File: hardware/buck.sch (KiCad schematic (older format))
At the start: 13 parts, among them U5 MP1584EN

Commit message: fix a silk screen error by swapping R14 and R15
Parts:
- renumbered R15 to R14, R14 to R15
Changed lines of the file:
@@
 P 4200 2500
 AR Path="/5C3476D8/5CA62D89" Ref="R?"  Part="1"
-AR Path="/5CA65CC5/5CA62D89" Ref="R14"  Part="1"
-F 0 "R14" H 4270 2546 50  0000 L CNN
+AR Path="/5CA65CC5/5CA62D89" Ref="R15"  Part="1"
+F 0 "R15" H 4270 2546 50  0000 L CNN
 F 1 "40.2k" H 4270 2455 50  0000 L CNN
 F 2 "Resistor_SMD:R_0603_1608Metric_Pad1.05x0.95mm_HandSolder" V 4130 2500 50  0001 C CNN
@@
 P 4550 2350
 AR Path="/5C3476D8/5CA62D90" Ref="R?"  Part="1"
-AR Path="/5CA65CC5/5CA62D90" Ref="R15"  Part="1"
-F 0 "R15" V 4757 2350 50  0000 C CNN
+AR Path="/5CA65CC5/5CA62D90" Ref="R14"  Part="1"
+F 0 "R14" V 4757 2350 50  0000 C CNN
 F 1 "210k" V 4666 2350 50  0000 C CNN
 F 2 "Resistor_SMD:R_0603_1608Metric_Pad1.05x0.95mm_HandSolder" V 4480 2350 50  0001 C CNN

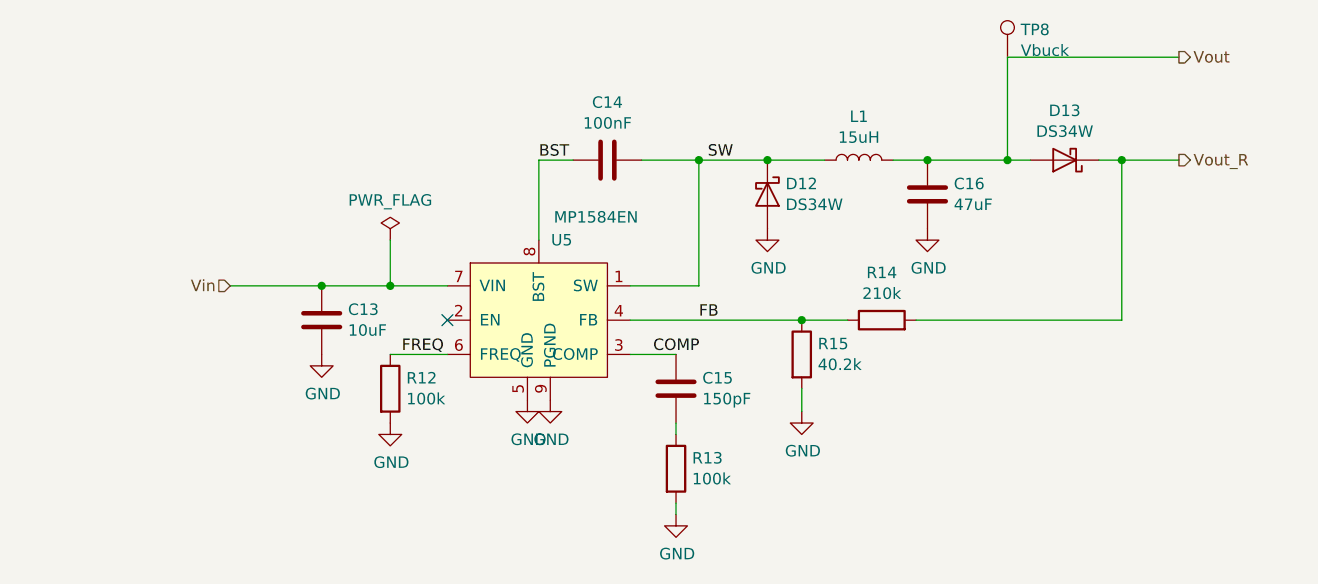
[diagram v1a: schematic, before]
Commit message: Changed to pure-serial topology. Changed to beefier mcu.
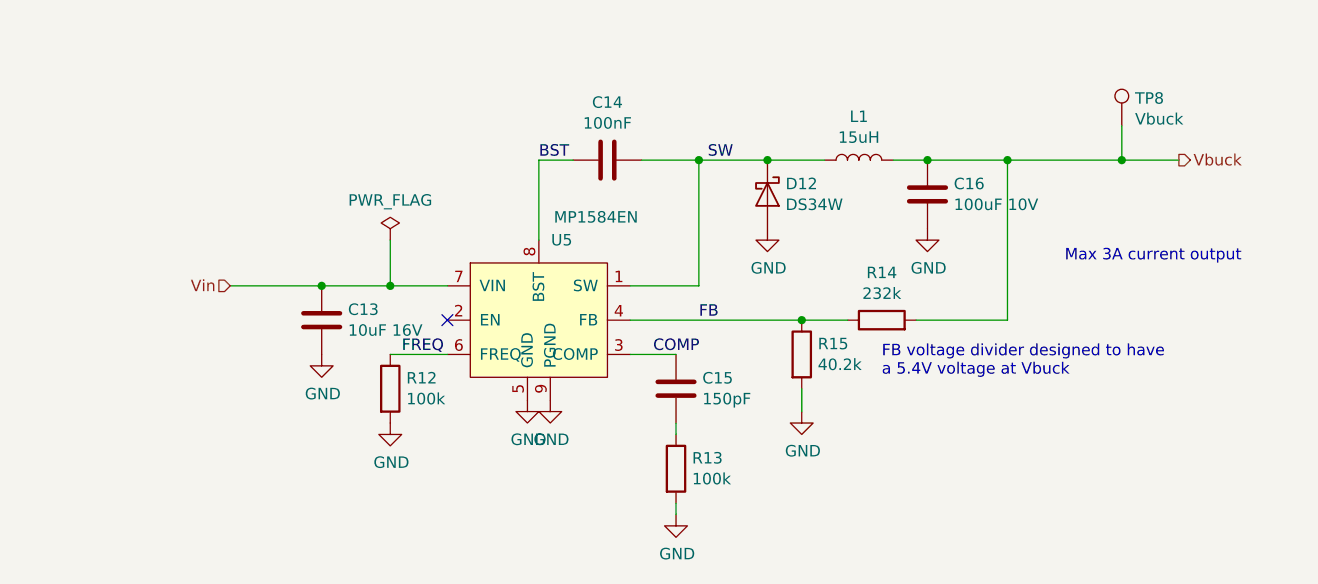
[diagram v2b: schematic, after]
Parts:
- removed D13: DS34W, Diode_SMD:D_SOD-123F, symbol Device:D_Schottky
- C13: value 10uF -> 10uF 16V
- C16: value 47uF -> 100uF 10V; footprint Capacitor_SMD:C_0805_2012Metric_Pad1.15x1.40mm_HandSolder -> Capacitor_SMD:C_1210_3225Metric_Pad1.42x2.65mm_HandSolder
- R14: value 210k -> 232k
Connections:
- net Vout_R is gone; now on net Vbuck: R14.2
- net Vout renamed Vbuck
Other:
- note added: "FB voltage divider designed to have\na 5.4V voltage at Vbuck"
- note added: "Max 3A current output"
- moved on the sheet: TP8
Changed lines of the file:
@@
-EESchema Schematic File Version 4
+EESchema Schematic File Version 5
 LIBS:pi-supercap-ups-cache
-EELAYER 26 0
+EELAYER 30 0
 EELAYER END
 $Descr A4 11693 8268
 encoding utf-8
-Sheet 6 8
+Sheet 8 8
 Title ""
 Date ""
@@
 AR Path="/5CA65CC5/5CA62D4C" Ref="C13"  Part="1"
 F 0 "C13" H 2215 2396 50  0000 L CNN
-F 1 "10uF" H 2215 2305 50  0000 L CNN
+F 1 "10uF 16V" H 2215 2305 50  0000 L CNN
 F 2 "Capacitor_SMD:C_0805_2012Metric_Pad1.15x1.40mm_HandSolder" H 2138 2200 50  0001 C CNN
 F 3 "~" H 2100 2350 50  0001 C CNN
@@
 AR Path="/5CA65CC5/5CA62D82" Ref="C16"  Part="1"
 F 0 "C16" H 4865 1846 50  0000 L CNN
-F 1 "47uF" H 4865 1755 50  0000 L CNN
-F 2 "Capacitor_SMD:C_0805_2012Metric_Pad1.15x1.40mm_HandSolder" H 4788 1650 50  0001 C CNN
+F 1 "100uF 10V" H 4865 1755 50  0000 L CNN
+F 2 "Capacitor_SMD:C_1210_3225Metric_Pad1.42x2.65mm_HandSolder" H 4788 1650 50  0001 C CNN
 F 3 "~" H 4750 1800 50  0001 C CNN
 F 4 "Min 6.3V" H 4750 1800 50  0001 C CNN "Notes"
@@
 AR Path="/5CA65CC5/5CA62D90" Ref="R14"  Part="1"
 F 0 "R14" V 4757 2350 50  0000 C CNN
-F 1 "210k" V 4666 2350 50  0000 C CNN
+F 1 "232k" V 4666 2350 50  0000 C CNN
 F 2 "Resistor_SMD:R_0603_1608Metric_Pad1.05x0.95mm_HandSolder" V 4480 2350 50  0001 C CNN
 F 3 "~" H 4550 2350 50  0001 C CNN
@@
 	3450 2350 4200 2350
 Wire Wire Line
-	4700 2350 5600 2350
+	4700 2350 5100 2350
 Wire Wire Line
 	3750 1650 3750 2200
-Wire Wire Line
-	5600 1650 5600 2350
 Wire Wire Line
 	3500 1650 3750 1650
@@
 Wire Wire Line
 	4200 2350 4400 2350
-Connection ~ 5600 1650
-Wire Wire Line
-	5600 1650 5850 1650
 Connection ~ 4050 1650
 Wire Wire Line
@@
 Text HLabel 1700 2200 0    50   Input ~ 0
 Vin
-$Comp
-L Device:D_Schottky D?
-U 1 1 5CA8EF52
-P 5350 1650
-AR Path="/5C345D5A/5CA8EF52" Ref="D?"  Part="1"
-AR Path="/5CA8EF52" Ref="D?"  Part="1"
-AR Path="/5CA65CC5/5CA8EF52" Ref="D13"  Part="1"
-F 0 "D13" H 5350 1434 50  0000 C CNN
-F 1 "DS34W" H 5350 1525 50  0000 C CNN
-F 2 "Diode_SMD:D_SOD-123F" H 5350 1650 50  0001 C CNN
-F 3 "~" H 5350 1650 50  0001 C CNN
-F 4 "Min current 3A" H 5350 1650 50  0001 C CNN "Notes"
-	1    5350 1650
-	-1   0    0    1
-$EndComp
 Connection ~ 4750 1650
-Wire Wire Line
-	5500 1650 5600 1650
 Text HLabel 5850 1650 2    50   Output ~ 0
-Vout_R
+Vbuck
 Wire Wire Line
 	4750 1650 5100 1650
-Text HLabel 5850 1200 2    50   Output ~ 0
-Vout
-Wire Wire Line
-	5850 1200 5100 1200
-Wire Wire Line
-	5100 1200 5100 1650
 Connection ~ 5100 1650
-Wire Wire Line
-	5100 1650 5200 1650
 $Comp
 L Connector:TestPoint TP?
 U 1 1 5CAACEED
-P 5100 1200
+P 5600 1500
 AR Path="/5C345D5A/5CAACEED" Ref="TP?"  Part="1"
 AR Path="/5CA65CC5/5CAACEED" Ref="TP8"  Part="1"
-F 0 "TP8" H 5158 1320 50  0000 L CNN
-F 1 "Vbuck" H 5158 1229 50  0000 L CNN
-F 2 "TestPoint:TestPoint_Keystone_5000-5004_Miniature" H 5300 1200 50  0001 C CNN
-F 3 "~" H 5300 1200 50  0001 C CNN
-	1    5100 1200
+F 0 "TP8" H 5658 1620 50  0000 L CNN
+F 1 "Vbuck" H 5658 1529 50  0000 L CNN
+F 2 "TestPoint:TestPoint_Keystone_5000-5004_Miniature" H 5800 1500 50  0001 C CNN
+F 3 "~" H 5800 1500 50  0001 C CNN
+	1    5600 1500
 	1    0    0    -1
 $EndComp
@@
 	1    0    0    -1
 $EndComp
+Wire Wire Line
+	5100 1650 5100 2350
+Text Notes 4550 2600 0    50   ~ 0
+FB voltage divider designed to have\na 5.4V voltage at Vbuck
+Wire Wire Line
+	5600 1500 5600 1650
+Connection ~ 5600 1650
+Wire Wire Line
+	5600 1650 5850 1650
+Text Notes 5350 2100 0    50   ~ 0
+Max 3A current output
+Wire Wire Line
+	5100 1650 5600 1650
 $EndSCHEMATC

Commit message: Layout partially done before change of plans
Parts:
- C13: value 10uF 16V -> 10uF 50V
- C16: value 100uF 10V -> 22uF 6.3V; footprint Capacitor_SMD:C_1210_3225Metric_Pad1.42x2.65mm_HandSolder -> Capacitor_SMD:C_0603_1608Metric_Pad1.05x0.95mm_HandSolder
- L1: value 15uH -> 10uH 3.5A; footprint CSAB0630-100M:INDC6060X300 -> custom:L_TDK_SLF10165_HandSolder; Part (none) -> TDK SLF10165T-100M3R8-3PF; URL (none) -> https://lcsc.com/product-detail/Inductors-SMD_TDK_SLF10165T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
- R12: value 100k -> 200k
- R13: value 100k -> 54.9k
- R14: value 232k -> 93k
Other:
- note added: "FB voltage divider designed to have\na 2.65V voltage at Vbuck"
- note removed: "FB voltage divider designed to have\na 5.4V voltage at Vbuck"
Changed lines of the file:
@@
 $Descr A4 11693 8268
 encoding utf-8
-Sheet 8 8
+Sheet 6 6
 Title ""
 Date ""
@@
 Comment3 ""
 Comment4 ""
+Comment5 ""
+Comment6 ""
+Comment7 ""
+Comment8 ""
+Comment9 ""
 $EndDescr
 $Comp
@@
 AR Path="/5CA65CC5/5CA62D4C" Ref="C13"  Part="1"
 F 0 "C13" H 2215 2396 50  0000 L CNN
-F 1 "10uF 16V" H 2215 2305 50  0000 L CNN
+F 1 "10uF 50V" H 2215 2305 50  0000 L CNN
 F 2 "Capacitor_SMD:C_0805_2012Metric_Pad1.15x1.40mm_HandSolder" H 2138 2200 50  0001 C CNN
 F 3 "~" H 2100 2350 50  0001 C CNN
@@
 AR Path="/5CA65CC5/5CA62D59" Ref="R12"  Part="1"
 F 0 "R12" H 2470 2696 50  0000 L CNN
-F 1 "100k" H 2470 2605 50  0000 L CNN
+F 1 "200k" H 2470 2605 50  0000 L CNN
 F 2 "Resistor_SMD:R_0603_1608Metric_Pad1.05x0.95mm_HandSolder" V 2330 2650 50  0001 C CNN
 F 3 "~" H 2400 2650 50  0001 C CNN
@@
 AR Path="/5CA65CC5/5CA62D7A" Ref="L1"  Part="1"
 F 0 "L1" V 4640 1650 50  0000 C CNN
-F 1 "15uH" V 4549 1650 50  0000 C CNN
-F 2 "CSAB0630-100M:INDC6060X300" H 4450 1650 50  0001 C CNN
+F 1 "10uH 3.5A" V 4549 1650 50  0000 C CNN
+F 2 "custom:L_TDK_SLF10165_HandSolder" H 4450 1650 50  0001 C CNN
 F 3 "~" H 4450 1650 50  0001 C CNN
+F 4 "https://lcsc.com/product-detail/Inductors-SMD_TDK_SLF10165T-100M3R8-3PF_TDK-SLF10165T-100M3R8-3PF_C91527.html" V 4450 1650 50  0001 C CNN "URL"
+F 5 "TDK SLF10165T-100M3R8-3PF" V 4450 1650 50  0001 C CNN "Part"
 	1    4450 1650
 	0    -1   -1   0
@@
 AR Path="/5CA65CC5/5CA62D82" Ref="C16"  Part="1"
 F 0 "C16" H 4865 1846 50  0000 L CNN
-F 1 "100uF 10V" H 4865 1755 50  0000 L CNN
-F 2 "Capacitor_SMD:C_1210_3225Metric_Pad1.42x2.65mm_HandSolder" H 4788 1650 50  0001 C CNN
+F 1 "22uF 6.3V" H 4865 1755 50  0000 L CNN
+F 2 "Capacitor_SMD:C_0603_1608Metric_Pad1.05x0.95mm_HandSolder" H 4788 1650 50  0001 C CNN
 F 3 "~" H 4750 1800 50  0001 C CNN
 F 4 "Min 6.3V" H 4750 1800 50  0001 C CNN "Notes"
@@
 AR Path="/5CA65CC5/5CA62D90" Ref="R14"  Part="1"
 F 0 "R14" V 4757 2350 50  0000 C CNN
-F 1 "232k" V 4666 2350 50  0000 C CNN
+F 1 "93k" V 4666 2350 50  0000 C CNN
 F 2 "Resistor_SMD:R_0603_1608Metric_Pad1.05x0.95mm_HandSolder" V 4480 2350 50  0001 C CNN
 F 3 "~" H 4550 2350 50  0001 C CNN
@@
 AR Path="/5CA65CC5/5CA62D9F" Ref="R13"  Part="1"
 F 0 "R13" H 3720 3046 50  0000 L CNN
-F 1 "100k" H 3720 2955 50  0000 L CNN
+F 1 "54.9k" H 3720 2955 50  0000 L CNN
 F 2 "Resistor_SMD:R_0603_1608Metric_Pad1.05x0.95mm_HandSolder" V 3580 3000 50  0001 C CNN
 F 3 "~" H 3650 3000 50  0001 C CNN
@@
 	5100 1650 5100 2350
 Text Notes 4550 2600 0    50   ~ 0
-FB voltage divider designed to have\na 5.4V voltage at Vbuck
+FB voltage divider designed to have\na 2.65V voltage at Vbuck
 Wire Wire Line
 	5600 1500 5600 1650

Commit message: revE ready for production
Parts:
- L1: footprint custom:L_TDK_SLF10165_HandSolder -> Inductor_SMD:L_Abracon_ASPI-0630LR; Part TDK SLF10165T-100M3R8-3PF -> Shun Xiang Nuo Elec SMMS0630-4R7M; URL https://lcsc.com/product-detail/Inductors-SMD_TDK_SLF10165T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 -> (none)
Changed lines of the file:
@@
 $Descr A4 11693 8268
 encoding utf-8
-Sheet 6 6
+Sheet 6 7
 Title ""
 Date ""
@@
 F 0 "L1" V 4640 1650 50  0000 C CNN
 F 1 "10uH 3.5A" V 4549 1650 50  0000 C CNN
-F 2 "custom:L_TDK_SLF10165_HandSolder" H 4450 1650 50  0001 C CNN
+F 2 "Inductor_SMD:L_Abracon_ASPI-0630LR" H 4450 1650 50  0001 C CNN
 F 3 "~" H 4450 1650 50  0001 C CNN
-F 4 "https://lcsc.com/product-detail/Inductors-SMD_TDK_SLF10165T-100M3R8-3PF_TDK-SLF10165T-100M3R8-3PF_C91527.html" V 4450 1650 50  0001 C CNN "URL"
-F 5 "TDK SLF10165T-100M3R8-3PF" V 4450 1650 50  0001 C CNN "Part"
+F 4 "" V 4450 1650 50  0001 C CNN "URL"
+F 5 "Shun Xiang Nuo Elec SMMS0630-4R7M" V 4450 1650 50  0001 C CNN "Part"
 	1    4450 1650
 	0    -1   -1   0

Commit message: Fixed wrong footprints & passive component values.
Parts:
- C13: footprint Capacitor_SMD:C_0805_2012Metric_Pad1.15x1.40mm_HandSolder -> Capacitor_SMD:C_1206_3216Metric_Pad1.42x1.75mm_HandSolder
- C16: value 22uF 6.3V -> 47uF 6.3V; footprint Capacitor_SMD:C_0603_1608Metric_Pad1.05x0.95mm_HandSolder -> Capacitor_SMD:C_0805_2012Metric_Pad1.15x1.40mm_HandSolder
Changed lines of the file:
@@
 F 0 "C13" H 2215 2396 50  0000 L CNN
 F 1 "10uF 50V" H 2215 2305 50  0000 L CNN
-F 2 "Capacitor_SMD:C_0805_2012Metric_Pad1.15x1.40mm_HandSolder" H 2138 2200 50  0001 C CNN
+F 2 "Capacitor_SMD:C_1206_3216Metric_Pad1.42x1.75mm_HandSolder" H 2138 2200 50  0001 C CNN
 F 3 "~" H 2100 2350 50  0001 C CNN
 F 4 "50V" H 2100 2350 50  0001 C CNN "Notes"
@@
 AR Path="/5CA65CC5/5CA62D82" Ref="C16"  Part="1"
 F 0 "C16" H 4865 1846 50  0000 L CNN
-F 1 "22uF 6.3V" H 4865 1755 50  0000 L CNN
-F 2 "Capacitor_SMD:C_0603_1608Metric_Pad1.05x0.95mm_HandSolder" H 4788 1650 50  0001 C CNN
+F 1 "47uF 6.3V" H 4865 1755 50  0000 L CNN
+F 2 "Capacitor_SMD:C_0805_2012Metric_Pad1.15x1.40mm_HandSolder" H 4788 1650 50  0001 C CNN
 F 3 "~" H 4750 1800 50  0001 C CNN
 F 4 "Min 6.3V" H 4750 1800 50  0001 C CNN "Notes"

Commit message: Add ENIN trace to the PCB. Change input voltage dividers for 1.1V ref.
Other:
- moved on the sheet: C13
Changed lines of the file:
@@
 L Device:C C?
 U 1 1 5CA62D4C
-P 2100 2350
+P 1400 2350
 AR Path="/5C3476D8/5CA62D4C" Ref="C?"  Part="1"
 AR Path="/5CA65CC5/5CA62D4C" Ref="C13"  Part="1"
-F 0 "C13" H 2215 2396 50  0000 L CNN
-F 1 "10uF 50V" H 2215 2305 50  0000 L CNN
-F 2 "Capacitor_SMD:C_1206_3216Metric_Pad1.42x1.75mm_HandSolder" H 2138 2200 50  0001 C CNN
-F 3 "~" H 2100 2350 50  0001 C CNN
-F 4 "50V" H 2100 2350 50  0001 C CNN "Notes"
-	1    2100 2350
+F 0 "C13" H 1515 2396 50  0000 L CNN
+F 1 "10uF 50V" H 1515 2305 50  0000 L CNN
+F 2 "Capacitor_SMD:C_1206_3216Metric_Pad1.42x1.75mm_HandSolder" H 1438 2200 50  0001 C CNN
+F 3 "~" H 1400 2350 50  0001 C CNN
+F 4 "50V" H 1400 2350 50  0001 C CNN "Notes"
+	1    1400 2350
 	1    0    0    -1
 $EndComp
@@
 L power:GND #PWR?
 U 1 1 5CA62D53
-P 2100 2500
+P 1400 2500
 AR Path="/5CA62D53" Ref="#PWR?"  Part="1"
 AR Path="/5C3476D8/5CA62D53" Ref="#PWR?"  Part="1"
 AR Path="/5CA65CC5/5CA62D53" Ref="#PWR037"  Part="1"
-F 0 "#PWR037" H 2100 2250 50  0001 C CNN
-F 1 "GND" H 2105 2327 50  0000 C CNN
-F 2 "" H 2100 2500 50  0001 C CNN
-F 3 "" H 2100 2500 50  0001 C CNN
-	1    2100 2500
+F 0 "#PWR037" H 1400 2250 50  0001 C CNN
+F 1 "GND" H 1405 2327 50  0000 C CNN
+F 2 "" H 1400 2500 50  0001 C CNN
+F 3 "" H 1400 2500 50  0001 C CNN
+	1    1400 2500
 	1    0    0    -1
 $EndComp
@@
 	1    0    0    -1
 $EndComp
-NoConn ~ 2650 2350
 Wire Wire Line
 	2400 2500 2650 2500
@@
 	1    0    0    -1
 $EndComp
-Connection ~ 2100 2200
-Wire Wire Line
-	2100 2200 2400 2200
-Wire Wire Line
-	1700 2200 2100 2200
+Connection ~ 1400 2200
+Wire Wire Line
+	1400 2200 1700 2200
+Wire Wire Line
+	1000 2200 1400 2200
 $Comp
 L power:GND #PWR?
@@
 L power:PWR_FLAG #FLG?
 U 1 1 5CA62DDA
-P 2400 2000
+P 1700 2000
 AR Path="/5C3476D8/5CA62DDA" Ref="#FLG?"  Part="1"
 AR Path="/5CA65CC5/5CA62DDA" Ref="#FLG08"  Part="1"
-F 0 "#FLG08" H 2400 2075 50  0001 C CNN
-F 1 "PWR_FLAG" H 2400 2174 50  0000 C CNN
-F 2 "" H 2400 2000 50  0001 C CNN
-F 3 "~" H 2400 2000 50  0001 C CNN
-	1    2400 2000
-	1    0    0    -1
-$EndComp
-Wire Wire Line
-	2400 2000 2400 2200
-Connection ~ 2400 2200
-Wire Wire Line
-	2400 2200 2650 2200
+F 0 "#FLG08" H 1700 2075 50  0001 C CNN
+F 1 "PWR_FLAG" H 1700 2174 50  0000 C CNN
+F 2 "" H 1700 2000 50  0001 C CNN
+F 3 "~" H 1700 2000 50  0001 C CNN
+	1    1700 2000
+	1    0    0    -1
+$EndComp
+Wire Wire Line
+	1700 2000 1700 2200
+Connection ~ 1700 2200
+Wire Wire Line
+	1700 2200 2650 2200
 Text Label 3900 1650 2    50   ~ 0
 SW
@@
 Text Label 3050 1650 0    50   ~ 0
 BST
-Text HLabel 1700 2200 0    50   Input ~ 0
+Text HLabel 1000 2200 0    50   Input ~ 0
 Vin
 Connection ~ 4750 1650
@@
 Wire Wire Line
 	5100 1650 5600 1650
+NoConn ~ 2650 2350
 $EndSCHEMATC

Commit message: Fix component values etc
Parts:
- C16: value 47uF 6.3V -> 47uF 10V
- L1: value 10uH 3.5A -> 4.7uH 3.5A
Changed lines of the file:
@@
 AR Path="/5CA65CC5/5CA62D7A" Ref="L1"  Part="1"
 F 0 "L1" V 4640 1650 50  0000 C CNN
-F 1 "10uH 3.5A" V 4549 1650 50  0000 C CNN
+F 1 "4.7uH 3.5A" V 4549 1650 50  0000 C CNN
 F 2 "Inductor_SMD:L_Abracon_ASPI-0630LR" H 4450 1650 50  0001 C CNN
 F 3 "~" H 4450 1650 50  0001 C CNN
@@
 AR Path="/5CA65CC5/5CA62D82" Ref="C16"  Part="1"
 F 0 "C16" H 4865 1846 50  0000 L CNN
-F 1 "47uF 6.3V" H 4865 1755 50  0000 L CNN
+F 1 "47uF 10V" H 4865 1755 50  0000 L CNN
 F 2 "Capacitor_SMD:C_0805_2012Metric_Pad1.15x1.40mm_HandSolder" H 4788 1650 50  0001 C CNN
 F 3 "~" H 4750 1800 50  0001 C CNN
